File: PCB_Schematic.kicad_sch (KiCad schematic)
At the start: 34 parts, among them J1 USB_A, Q7 BSS138, Q8 BSS138, U2 LM1117-3.3, U3 TPS54331-Q1, U5 FT232RL, U6 STM32F091RCTx

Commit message: More Updates
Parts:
- removed U2: LM1117-3.3, symbol Regulator_Linear:LM1117-3.3
- added U2: LM1117MP-ADJ, Package_TO_SOT_SMD:SOT-223-3_TabPin2, symbol Regulator_Linear:LM1117MP-ADJ
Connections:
- net VBUS is gone; now on net +5V: Cin.1, U3.2 (VIN)
- net +3.3V: now also U6.13 (VDDA), U6.19 (VDD), U6.64 (VDD), U2.2 (VO)
- net +5V: now also U2.3 (VI)
- net at R1.2, R2.1: now also U2.1 (ADJ)
- no-connect marks 54 -> 56
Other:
- moved on the sheet: C1, C2, C3, C4, C5, D2, D3, J1, J_IMU1, J_IMU2, R1, R2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

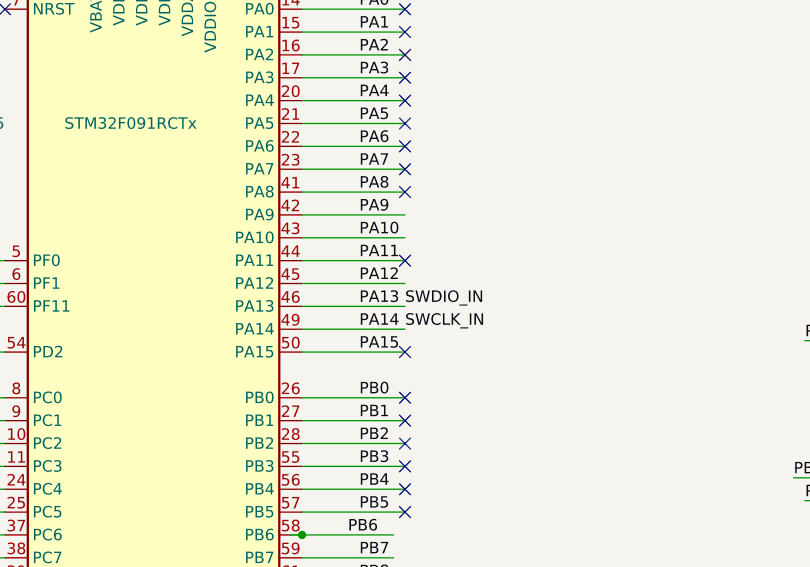
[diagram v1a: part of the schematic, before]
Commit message: Add some decaps for 3.3V
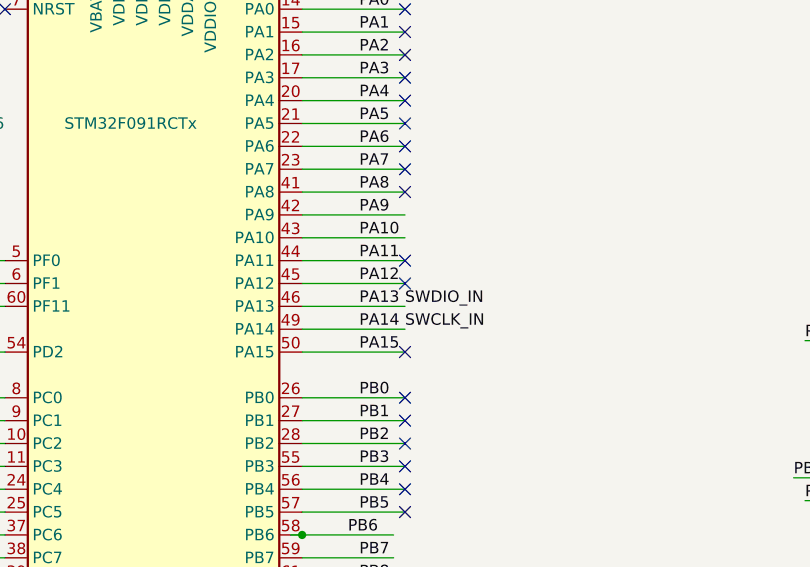
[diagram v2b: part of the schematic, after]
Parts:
- U3: footprint (none) -> Package_SO:TI_SO-PowerPAD-8_ThermalVias
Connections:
- no-connect marks 56 -> 57
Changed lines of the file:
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@@
 	)
 	(no_connect
+		(at 194.31 107.95)
+	)
+	(no_connect
 		(at 138.43 156.21)
 	)
@@
 			)
 		)
-		(property "Datasheet" "https://mm.digikey.com/Volume0/opasdata/d220001/medias/docus/5534/USB-A1HSXX.pdf"
+		(property "Datasheet" "~"
 			(at 29.21 67.31 0)
 			(effects
@@
 			)
 		)
-		(property "Description" ""
+		(property "Description" "USB Type A connector"
 			(at 25.4 66.04 0)
 			(effects
@@
 			)
 		)
-		(property "Footprint" ""
+		(property "Footprint" "Package_SO:TI_SO-PowerPAD-8_ThermalVias"
 			(at 116.84 35.56 0)
 			(effects
@@
 			)
 		)
-		(property "Datasheet" "https://www.ti.com/lit/ds/symlink/tps54331-q1.pdf?ts=1727123204197"
+		(property "Datasheet" "http://www.ti.com/lit/ds/symlink/tps54336a.pdf"
 			(at 119.38 38.1 0)
 			(effects
@@
 			)
 		)
-		(property "Description" ""
+		(property "Description" "4.5V to 28V Input, 3A, Synchronous Step-Down Converter with Eco-mode(tm)"
 			(at 93.98 26.67 0)
 			(effects
@@
 			)
 		)
-		(property "Description" ""
+		(property "Description" "50V Vds, 0.22A Id, N-Channel MOSFET, SOT-23"
 			(at 222.25 62.23 0)
 			(effects

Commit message: Stuff
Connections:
- net PA10: no longer U5.1 (TXD)
- net PA9: no longer U5.5 (RXD)
- net PC12: now also U5.5 (RXD)
- net PD2: now also U5.1 (TXD)
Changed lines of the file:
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@@
-		)
-	)
-	(label "PA9"
-		(at 78.74 137.16 0)
-		(fields_autoplaced yes)
-		(effects
-			(font
-				(size 1.27 1.27)
-			)
-			(justify left bottom)
 		)
 	)
@@
 		)
 	)
+	(label "PD2"
+		(at 78.74 134.62 0)
+		(fields_autoplaced yes)
+		(effects
+			(font
+				(size 1.27 1.27)
+			)
+			(justify left bottom)
+		)
+	)
 	(label "PA4"
 		(at 189.23 87.63 0)
@@
 		)
 	)
+	(label "PC12"
+		(at 78.74 137.16 0)
+		(fields_autoplaced yes)
+		(effects
+			(font
+				(size 1.27 1.27)
+			)
+			(justify left bottom)
+		)
+	)
 	(label "PC6"
 		(at 140.97 135.89 0)
@@
 		(fields_autoplaced yes)
 		(effects
-			(font
-				(size 1.27 1.27)
-			)
-			(justify left bottom)
-		)
-	)
-	(label "PA10"
-		(at 78.74 134.62 0)
-		(fields_autoplaced yes)
-		(effects

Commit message: Sam
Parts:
- removed Q8: BSS138, Package_TO_SOT_SMD:SOT-23, symbol Transistor_FET:BSS138
- removed R5, R6: 10k, symbol Device:R
- added J2: Conn_01x04_Pin, symbol Connector:Conn_01x04_Pin
- renumbered Cboot to Cboot1, Ccomp to Ccomp1, Cin to Cin1, Cout to Cout1, Css to Css1, J_Ultrasonic to J_Ultrasonic1, Rcomp to Rcomp1, Rfbb to Rfbb1, Rfbt to Rfbt1
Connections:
- net +5V: now also J_Ultrasonic1.1 (Pin_1)
- net PB7: now also J_Ultrasonic1.3 (Pin_3)

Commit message: new stuff
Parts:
- removed J_IMU1, J_IMU2, J_Ultrasonic1: Conn_01x04_Female, symbol Connector:Conn_01x04_Female
- added J_Ultrasonic1, J_Ultrasonic2: Conn_01x04_Pin, Library:CONN_B4B-XH-A_JSTProject, symbol Connector:Conn_01x04_Pin
- J_Ultrasonic: renamed from J2; footprint (none) -> Library:CONN_B4B-XH-A_JSTProject
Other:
- moved on the sheet: J_Ultrasonic
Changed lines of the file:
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@@
+	)
+	(symbol
+		(lib_id "Connector:Conn_01x04_Pin")
+		(at 250.19 127 0)
+		(unit 1)
+		(exclude_from_sim no)
+		(in_bom yes)
+		(on_board yes)
+		(dnp no)
+		(property "Reference" "J_Ultrasonic2"
+			(at 262.636 125.73 0)
+			(effects
+				(font
+					(size 1.27 1.27)
+				)
+			)
+		)
+		(property "Value" "Conn_01x04_Pin"
+			(at 264.414 128.27 0)
+			(effects
+				(font
+					(size 1.27 1.27)
+				)
+			)
+		)
+		(property "Footprint" "Library:CONN_B4B-XH-A_JSTProject"
+			(at 250.19 127 0)
+			(effects
+				(font
+					(size 1.27 1.27)
+				)
+				(hide yes)
+			)
+		)
+		(property "Datasheet" "~"
+			(at 250.19 127 0)
+			(effects
+				(font
+					(size 1.27 1.27)
+				)
+				(hide yes)
+			)
+		)
+		(property "Description" "Generic connector, single row, 01x04, script generated"
+			(at 250.19 127 0)
+			(effects
+				(font
+					(size 1.27 1.27)
+				)
+				(hide yes)
+			)
+		)
+		(pin "3"
+		)
+		(pin "2"
+		)
+		(pin "1"
+		)
+		(pin "4"
+		)
+		(instances
+			(project "PCB_Schematic"
+				(path "/a0c17764-e0d1-4df5-b871-1489cf266494"
+					(reference "J_Ultrasonic2")
+					(unit 1)
+				)
+			)
+		)
 	)
 	(symbol
@@
 	)
 	(symbol
-		(lib_id "Connector:Conn_01x04_Female")
-		(at 255.27 111.76 0)
-		(unit 1)
-		(exclude_from_sim no)
-		(in_bom yes)
-		(on_board yes)
-		(dnp no)
-		(fields_autoplaced yes)
-		(property "Reference" "J_IMU1"
-			(at 256.54 111.7599 0)
-			(effects
-				(font
-					(size 1.27 1.27)
-				)
-				(justify left)
-			)
-		)
-		(property "Value" "Conn_01x04_Female"
-			(at 256.54 114.2999 0)
-			(effects
-				(font
-					(size 1.27 1.27)
-				)
-				(justify left)
-			)
-		)
-		(property "Footprint" ""
-			(at 255.27 111.76 0)
-			(effects
-				(font
-					(size 1.27 1.27)
-				)
-				(hide yes)
-			)
-		)
-		(property "Datasheet" "~"
-			(at 255.27 111.76 0)
-			(effects
-				(font
-					(size 1.27 1.27)
-				)
-				(hide yes)
-			)
-		)
-		(property "Description" ""
-			(at 255.27 111.76 0)
-			(effects
-				(font
-					(size 1.27 1.27)
-				)
-				(hide yes)
-			)
-		)
-		(pin "1"
-		)
-		(pin "2"
-		)
-		(pin "3"
-		)
-		(pin "4"
-		)
-		(instances
-			(project ""
-				(path "/a0c17764-e0d1-4df5-b871-1489cf266494"
-					(reference "J_IMU1")
-					(unit 1)
-				)
-			)
-		)
-	)
-	(symbol
 		(lib_id "Device:C_Polarized_US")
 		(at 58.42 77.47 0)
@@
 	(symbol
 		(lib_id "Connector:Conn_01x04_Pin")
-		(at 237.49 74.93 0)
-		(unit 1)
-		(exclude_from_sim no)
-		(in_bom yes)
-		(on_board yes)
-		(dnp no)
-		(fields_autoplaced yes)
-		(property "Reference" "J2"
-			(at 238.125 67.31 0)
+		(at 255.27 43.18 0)
+		(unit 1)
+		(exclude_from_sim no)
+		(in_bom yes)
+		(on_board yes)
+		(dnp no)
+		(fields_autoplaced yes)
+		(property "Reference" "J_Ultrasonic"
+			(at 255.905 35.56 0)
 			(effects
 				(font
@@
 		)
 		(property "Value" "Conn_01x04_Pin"
-			(at 238.125 69.85 0)
-			(effects
-				(font
-					(size 1.27 1.27)
-				)
-			)
-		)
-		(property "Footprint" ""
-			(at 237.49 74.93 0)
+			(at 255.905 38.1 0)
+			(effects
+				(font
+					(size 1.27 1.27)
+				)
+			)
+		)
+		(property "Footprint" "Library:CONN_B4B-XH-A_JSTProject"
+			(at 255.27 43.18 0)
 			(effects
 				(font
@@
 		)
 		(property "Datasheet" "~"
-			(at 237.49 74.93 0)
+			(at 255.27 43.18 0)
 			(effects
 				(font
@@
 		)
 		(property "Description" "Generic connector, single row, 01x04, script generated"
-			(at 237.49 74.93 0)
+			(at 255.27 43.18 0)
 			(effects
 				(font
@@
 			(project ""
 				(path "/a0c17764-e0d1-4df5-b871-1489cf266494"
-					(reference "J2")
+					(reference "J_Ultrasonic")
 					(unit 1)
 				)
@@
 	)
 	(symbol
-		(lib_id "Connector:Conn_01x04_Female")
-		(at 255.27 127 0)
-		(unit 1)
-		(exclude_from_sim no)
-		(in_bom yes)
-		(on_board yes)
-		(dnp no)
-		(fields_autoplaced yes)
-		(property "Reference" "J_IMU2"
-			(at 256.54 126.9999 0)
-			(effects
-				(font
-					(size 1.27 1.27)
-				)
-				(justify left)
-			)
-		)
-		(property "Value" "Conn_01x04_Female"
-			(at 256.54 129.5399 0)
-			(effects
-				(font
-					(size 1.27 1.27)
-				)
-				(justify left)
-			)
-		)
-		(property "Footprint" ""
-			(at 255.27 127 0)
-			(effects
-				(font
-					(size 1.27 1.27)
-				)
-				(hide yes)
-			)
-		)
-		(property "Datasheet" "~"
-			(at 255.27 127 0)
-			(effects
-				(font
-					(size 1.27 1.27)
-				)
-				(hide yes)
-			)
-		)
-		(property "Description" ""
-			(at 255.27 127 0)
-			(effects
-				(font
-					(size 1.27 1.27)
-				)
-				(hide yes)
-			)
-		)
-		(pin "1"
-		)
-		(pin "2"
-		)
-		(pin "3"
-		)
-		(pin "4"
-		)
-		(instances
-			(project ""
-				(path "/a0c17764-e0d1-4df5-b871-1489cf266494"
-					(reference "J_IMU2")
-					(unit 1)
-				)
-			)
-		)
-	)
-	(symbol
 		(lib_id "power:GND")
 		(at 134.62 34.29 0)
@@
 	)
 	(symbol
-		(lib_id "Connector:Conn_01x04_Female")
-		(at 260.35 43.18 0)
-		(unit 1)
-		(exclude_from_sim no)
-		(in_bom yes)
-		(on_board yes)
-		(dnp no)
-		(fields_autoplaced yes)
+		(lib_id "Connector:Conn_01x04_Pin")
+		(at 250.19 111.76 0)
+		(unit 1)
+		(exclude_from_sim no)
+		(in_bom yes)
+		(on_board yes)
+		(dnp no)
 		(property "Reference" "J_Ultrasonic1"
-			(at 261.62 43.1799 0)
-			(effects
-				(font
-					(size 1.27 1.27)
-				)
-				(justify left)
-			)
-		)
-		(property "Value" "Conn_01x04_Female"
-			(at 261.62 45.7199 0)
-			(effects
-				(font
-					(size 1.27 1.27)
-				)
-				(justify left)
-			)
-		)
-		(property "Footprint" ""
-			(at 260.35 43.18 0)
+			(at 264.668 112.522 0)
+			(effects
+				(font
+					(size 1.27 1.27)
+				)
+			)
+		)
+		(property "Value" "Conn_01x04_Pin"
+			(at 265.43 114.808 0)
+			(effects
+				(font
+					(size 1.27 1.27)
+				)
+			)
+		)
+		(property "Footprint" "Library:CONN_B4B-XH-A_JSTProject"
+			(at 250.19 111.76 0)
 			(effects
 				(font
@@
 		)
 		(property "Datasheet" "~"
-			(at 260.35 43.18 0)
-			(effects
-				(font
-					(size 1.27 1.27)
-				)
-				(hide yes)
-			)
-		)
-		(property "Description" ""
-			(at 260.35 43.18 0)
-			(effects
-				(font
-					(size 1.27 1.27)
-				)
-				(hide yes)
-			)
-		)
-		(pin "1"
+			(at 250.19 111.76 0)
+			(effects
+				(font
+					(size 1.27 1.27)
+				)
+				(hide yes)
+			)
+		)
+		(property "Description" "Generic connector, single row, 01x04, script generated"
+			(at 250.19 111.76 0)
+			(effects
+				(font
+					(size 1.27 1.27)
+				)
+				(hide yes)
+			)
+		)
+		(pin "3"
 		)
 		(pin "2"
 		)
-		(pin "3"
+		(pin "1"
 		)
 		(pin "4"
 		)
 		(instances
-			(project ""
+			(project "PCB_Schematic"
 				(path "/a0c17764-e0d1-4df5-b871-1489cf266494"
 					(reference "J_Ultrasonic1")

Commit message: PCB Schematic Additions
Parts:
- added C10, C11: 12pF, Capacitor_SMD:C_0805_2012Metric_Pad1.15x1.40mm_HandSolder, symbol Device:C
- added C12, C13: 20pF, Capacitor_SMD:C_0805_2012Metric_Pad1.15x1.40mm_HandSolder, symbol Device:C
- added C14, C6, C7, C8, C9: .1 uF, symbol Device:C
- added D4: D_Schottky, symbol Device:D_Schottky
- added D5: BAT60AJFILM, Diode_SMD:D_SOD-323, symbol Diode:BAT60A
- added D6, D7, D8: LED, symbol Device:LED
- added J2: Conn_02x05_Odd_Even, symbol Connector_Generic:Conn_02x05_Odd_Even
- added J3, J4: Conn_02x03_Odd_Even, Connector_PinHeader_1.27mm:PinHeader_2x03_P1.27mm_Vertical, symbol Connector_Generic:Conn_02x03_Odd_Even
- added J_CS_Power: Conn_01x04_Pin, symbol Connector:Conn_01x04_Pin
- added R10: 390, Resistor_SMD:R_0805_2012Metric_Pad1.15x1.40mm_HandSolder, symbol Device:R_US
- added R11: 100K, symbol Device:R
- added R5, R6: 270, symbol Device:R
- added R7: 5.1k, symbol Device:R
- added R8, R9: 150, symbol Device:R
- added SW1: SW_Push, symbol Switch:SW_Push
- added X1: 32.768kHz(12.5pF), local_models:ECX-.327-CDX-1293, symbol Device:Crystal
- added X2: 8MHz(20pF), Crystal:Crystal_SMD_3225-4Pin_3.2x2.5mm, symbol Device:Crystal
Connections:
- net +3.3V: now also C6.1, C7.1, C8.1, C9.1, D7.2 (A), J_CS_Power.1 (Pin_1), J_CS_Power.2 (Pin_2), J_CS_Power.3 (Pin_3), J_CS_Power.4 (Pin_4), R11.1
- net +5V: now also D4.1 (K), D5.1 (K), D8.2 (A), R7.1; no longer J1.1 (VBUS)
- net GND: now also C10.2, C11.2, C12.2, C13.2, C14.2, C6.2, C7.2, C8.2, C9.2, D6.1 (K), J2.3 (Pin_3), J2.4 (Pin_4), R8.2, R9.2, SW1.1
- net PA13: now also J2.2 (Pin_2)
- net PA14: now also J2.6 (Pin_6)
- net PC14: now also J3.3 (Pin_3)
- net PC15: now also J3.4 (Pin_4)
- net PF0: now also J4.3 (Pin_3)
- net PF1: now also J4.4 (Pin_4)
- net at D3.1 (K): now also R6.1
- net at U5.22 (CBUS1): now also R6.2
- net at U5.23 (CBUS0): now also R5.2
- net at D2.1 (K): now also R5.1
- new net: C12.1, J4.5 (Pin_5), X2.1
- new net: C13.1, R10.2, X2.2
- new net: D7.1 (K), R9.1
- new net: C10.1, J3.5 (Pin_5), X1.1
- new net: D8.1 (K), R8.1
- new net: D4.2 (A), J1.1 (VBUS)
- new net: D6.2 (A), R7.2
- new net: C11.1, J3.6 (Pin_6), X1.2
- new net: J4.6 (Pin_6), R10.1
- new net NRST: C14.1, J2.1 (Pin_1), R11.2, SW1.2
- new net U5V: D5.2 (A), J2.10 (Pin_10), J2.9 (Pin_9)
- new net V3.3_IN: J2.7 (Pin_7), J2.8 (Pin_8)
- new net XPC14: J3.1 (Pin_1)
- new net XPC15: J3.2 (Pin_2)
- new net XPF0: J4.1 (Pin_1)
- new net XPF1: J4.2 (Pin_2)
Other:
- moved on the sheet: C1, C3, C4, C5, D2, D3, J_Ultrasonic, J_Ultrasonic1, J_Ultrasonic2, Q7, R3, R4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

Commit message: changes Sam
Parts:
- C1, C14, C2, C3, C4, C5, C6, C7, C8, C9, Cboot1, Ccomp1, Ccomp2, Cin1, Css1: footprint (none) -> Capacitor_SMD:C_1206_3216Metric_Pad1.33x1.80mm_HandSolder
- R1, R11, R2, R3, R4, R5, R6, R7, R8, R9, Rcomp1, Rfbb1, Rfbt1: footprint (none) -> Resistor_SMD:R_1206_3216Metric_Pad1.30x1.75mm_HandSolder
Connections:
- no-connect marks 57 -> 58
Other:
- moved on the sheet: C1, C10, C11, C12, C13, C14, C2, C3, C4, C5, C6, C7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

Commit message: Sam more bs
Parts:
- removed C10, C11: 12pF, Capacitor_SMD:C_0805_2012Metric_Pad1.15x1.40mm_HandSolder, symbol Device:C
- removed C12, C13: 20pF, Capacitor_SMD:C_0805_2012Metric_Pad1.15x1.40mm_HandSolder, symbol Device:C
- removed D5: BAT60AJFILM, Diode_SMD:D_SOD-323, symbol Diode:BAT60A
- removed D6: LED, symbol Device:LED
- removed J3, J4: Conn_02x03_Odd_Even, Connector_PinHeader_1.27mm:PinHeader_2x03_P1.27mm_Vertical, symbol Connector_Generic:Conn_02x03_Odd_Even
- removed R10: 390, Resistor_SMD:R_0805_2012Metric_Pad1.15x1.40mm_HandSolder, symbol Device:R_US
- removed R7: 5.1k, Resistor_SMD:R_1206_3216Metric_Pad1.30x1.75mm_HandSolder, symbol Device:R
- removed X1: 32.768kHz(12.5pF), local_models:ECX-.327-CDX-1293, symbol Device:Crystal
- removed X2: 8MHz(20pF), Crystal:Crystal_SMD_3225-4Pin_3.2x2.5mm, symbol Device:Crystal
- J1: renamed from J_Ultrasonic1; value Conn_01x04_Pin -> IMU_1
- J2: renamed from J_CS_Power; value Conn_01x04_Pin -> Power_Connector
- J7: renamed from J_Ultrasonic; value Conn_01x04_Pin -> Ultrasonic
- J8: renamed from J_Ultrasonic2; value Conn_01x04_Pin -> IMU_2
- renumbered J2 to J3, J1 to J6
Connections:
- net PB7 is gone; now on net Echo: U6.59 (PB7)
- net PB8 is gone; now on net SCL: U6.61 (PB8)
- net PB9 is gone; now on net SDA: U6.62 (PB9)
- net +3.3V: now also J1.1 (Pin_1), J8.1 (Pin_1)
- net +5V: now also D4.2 (A), J6.1 (VBUS), J7.1 (Pin_1); no longer D4.1 (K), D8.2 (A)
- net GND: now also J1.2 (Pin_2), J7.4 (Pin_4), J8.2 (Pin_2)
- net NRST: now also U6.7 (NRST)
- net Echo: now reaches Q7.3 (D), R4.2
- net Echo: now also J7.3 (Pin_3)
- net PA13 renamed SWDIO_IN
- net PA14 renamed SWCLK_IN
- net PB10 renamed SCL
- net SCL: now also J1.3 (Pin_3), J8.3 (Pin_3)
- net PB11 renamed SDA
- net SDA: now also J1.4 (Pin_4), J8.4 (Pin_4)
- net PB6: no longer names the net of Q7.2 (S), R3.2
- net PB6: no longer U6.58 (PB6)
- net U5V: no longer names the net of J3.10 (Pin_10)
- net U5V: no longer J3.9 (Pin_9)
- net V3.3_IN: no longer names the net of J3.7 (Pin_7)
- net V3.3_IN: no longer J3.8 (Pin_8)
- new net: D4.1 (K), D8.2 (A)
- new net Trig: J7.2 (Pin_2), U6.58 (PB6)
- no-connect marks 58 -> 63
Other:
- moved on the sheet: J1, J7, J8, Q7, R3, R4
